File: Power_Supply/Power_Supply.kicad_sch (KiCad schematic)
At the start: 62 parts, among them J1 ICSP, J2 Conn_01x01, J3 Conn_01x01, J4 Conn_01x02, SW1 UP, SW2 DW, SW3 V_I_SEL, SW4 O_EN, U1 L78L08_SOT89, U2 ATmega328PB-AU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

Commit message: schematic general changes
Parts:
- gave numbers to parts that had none: 1
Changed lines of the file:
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@@
   (symbol (lib_id "power:+5V") (at 177.8 130.81 0) (unit 1)
     (in_bom yes) (on_board yes)
-    (property "Reference" "#PWR?" (id 0) (at 177.8 134.62 0)
+    (property "Reference" "#PWR0138" (id 0) (at 177.8 134.62 0)
       (effects (font (size 1.27 1.27)) hide)
     )
@@
   (symbol (lib_id "power:GND") (at 172.72 133.35 0) (unit 1)
     (in_bom yes) (on_board yes)
-    (property "Reference" "#PWR?" (id 0) (at 172.72 139.7 0)
+    (property "Reference" "#PWR0139" (id 0) (at 172.72 139.7 0)
       (effects (font (size 1.27 1.27)) hide)
     )
@@
   (symbol (lib_id "Connector_Generic:Conn_01x07") (at 187.96 140.97 0) (unit 1)
     (in_bom yes) (on_board yes)
-    (property "Reference" "J?" (id 0) (at 190.5 139.7 0)
+    (property "Reference" "J5" (id 0) (at 190.5 139.7 0)
       (effects (font (size 1.27 1.27)) (justify left))
     )
@@
     )
     (path "/4d9958f2-beb5-4ed4-8a98-4e96ac27dafe"
-      (reference "#PWR?") (unit 1)
+      (reference "#PWR0138") (unit 1)
     )
     (path "/62210738-7293-4785-87bd-dc34d7328707"
-      (reference "#PWR?") (unit 1)
+      (reference "#PWR0139") (unit 1)
     )
     (path "/a216915c-7324-469c-8737-2c3edfb6ea67"
@@
     )
     (path "/4a5aceff-e57e-435c-ba37-61c44454879c"
-      (reference "J?") (unit 1)
+      (reference "J5") (unit 1)
     )
     (path "/93bb1d96-5265-4922-b320-5a7c229c525d"

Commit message: layout complete - OLED missing
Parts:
- removed C12, C7: 100nF, Capacitor_SMD:C_0805_2012Metric, symbol Device:C_Small
- removed J4: Conn_01x02, Custom_Vertical_1x_2.54mm_Pin_Header:PinHeader_1x02_P2.54mm_Vertical, symbol Connector_Generic:Conn_01x02
- added C? (x2): 10uF, Capacitor_SMD:C_Elec_5x5.4, symbol Device:CP_Small
- added H1, H2, H3, H4: MountingHole_Pad, MountingHole:MountingHole_2.2mm_M2_ISO7380_Pad, symbol Mechanical:MountingHole_Pad
- added J4: Screw_Terminal_01x02, TerminalBlock_Altech:Altech_AK300_1x02_P5.00mm_45-Degree, symbol Connector:Screw_Terminal_01x02
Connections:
- net SCL1 is gone; now on net SW4: U2.6 (PE1)
- net SDA1 is gone; now on net SW1: U2.3 (PE0)
- net +VSW: now also C?.2, J4.1 (Pin_1)
- net GND: now also C?.1, C?.1, H1.1, H2.1, H3.1, H4.1, J4.2 (Pin_2)
- net VDC: now also C?.2
- net SW1: now reaches R6.2, SW1.1
- net SW1: no longer U2.1 (PD3)
- net SW2: now reaches R8.2, SW2.1, U2.2 (PD4)
- net SW4: now reaches R10.2, SW4.1
- net SW4: no longer U2.10 (PD6)
- net SW3: now reaches R9.2, SW3.1
- net SW3: now also U2.1 (PD3); no longer U2.9 (PD5)

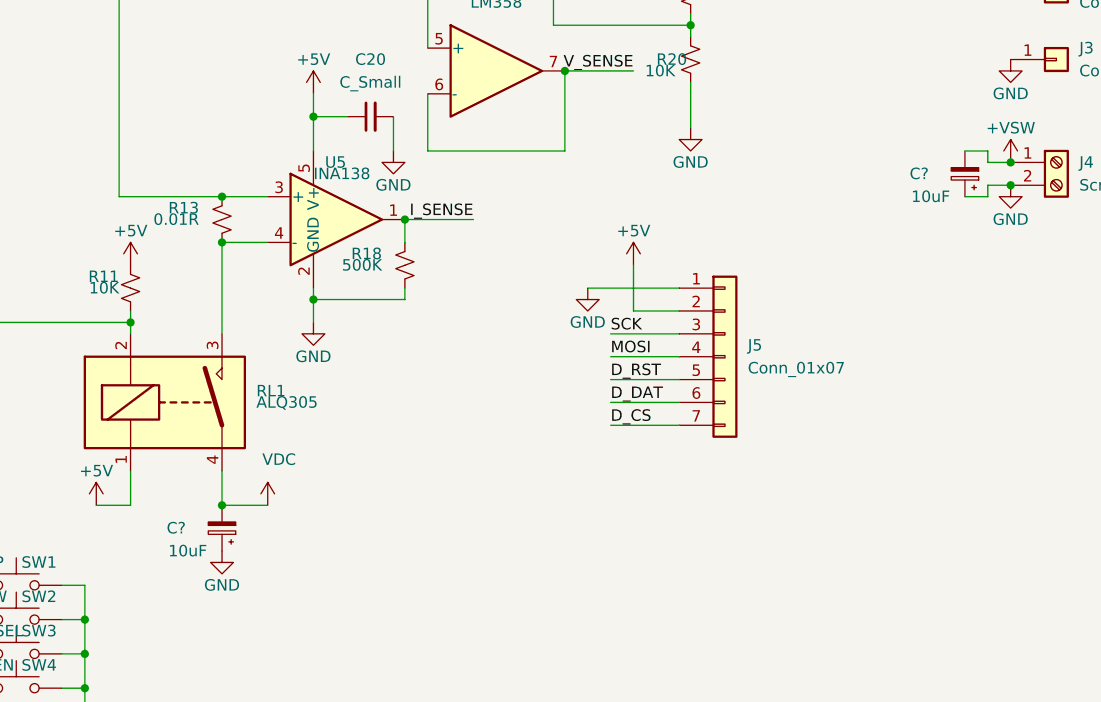
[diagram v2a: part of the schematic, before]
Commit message: schem - added bypass caps
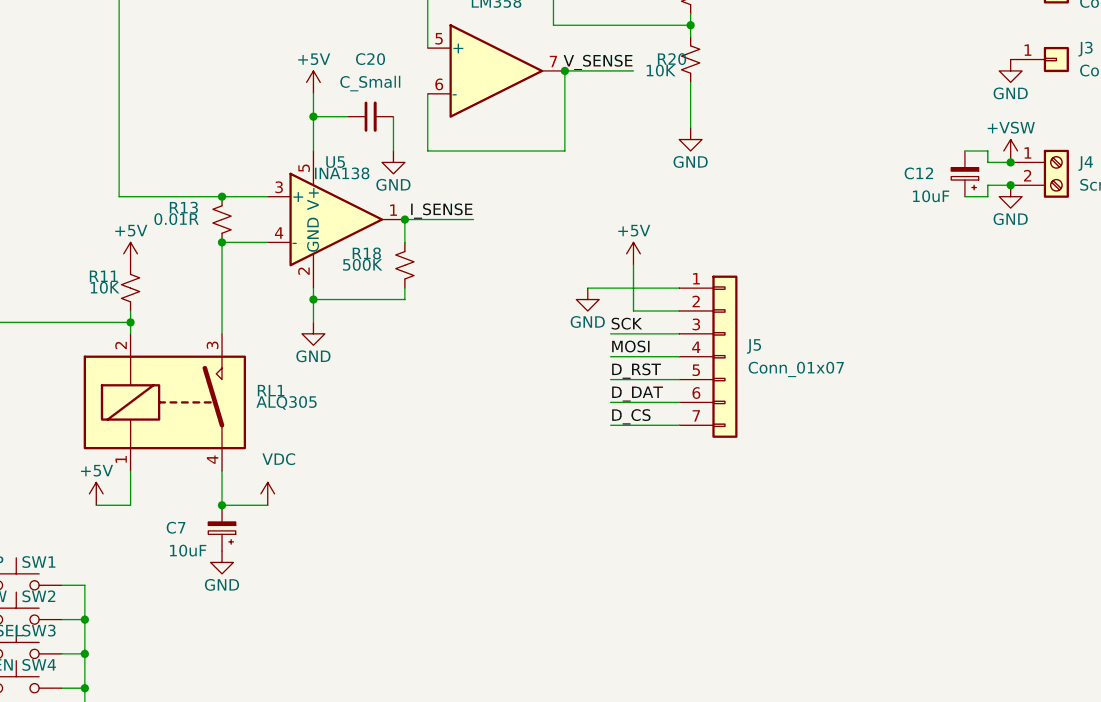
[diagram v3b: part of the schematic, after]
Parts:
- gave numbers to parts that had none: 2
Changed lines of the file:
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@@
   (symbol (lib_id "power:GND") (at 132.08 162.56 0) (unit 1)
     (in_bom yes) (on_board yes)
-    (property "Reference" "#PWR?" (id 0) (at 132.08 168.91 0)
+    (property "Reference" "#PWR0141" (id 0) (at 132.08 168.91 0)
       (effects (font (size 1.27 1.27)) hide)
     )
@@
   (symbol (lib_id "Device:CP_Small") (at 132.08 160.02 180) (unit 1)
     (in_bom yes) (on_board yes)
-    (property "Reference" "C?" (id 0) (at 127 160.02 0))
+    (property "Reference" "C7" (id 0) (at 127 160.02 0))
     (property "Value" "10uF" (id 1) (at 128.27 162.56 0))
     (property "Footprint" "Capacitor_SMD:C_Elec_5x5.4" (id 2) (at 132.08 160.02 0)
@@
   (symbol (lib_id "Device:CP_Small") (at 214.63 120.65 180) (unit 1)
     (in_bom yes) (on_board yes)
-    (property "Reference" "C?" (id 0) (at 209.55 120.65 0))
+    (property "Reference" "C12" (id 0) (at 209.55 120.65 0))
     (property "Value" "10uF" (id 1) (at 210.82 123.19 0))
     (property "Footprint" "Capacitor_SMD:C_Elec_5x5.4" (id 2) (at 214.63 120.65 0)
@@
     )
     (path "/255a29b3-3ad0-4a90-bdf9-643315723593"
-      (reference "#PWR?") (unit 1)
+      (reference "#PWR0141") (unit 1)
     )
     (path "/a216915c-7324-469c-8737-2c3edfb6ea67"
@@
       (reference "C6") (unit 1)
     )
+    (path "/311ae82b-454a-4b31-a9dc-b6314a74ab0d"
+      (reference "C7") (unit 1)
+    )
     (path "/232dade7-711c-48f9-ad1c-1fae503ac0aa"
       (reference "C8") (unit 1)
@@
       (reference "C11") (unit 1)
     )
+    (path "/80312307-f61e-439d-8183-53fd4206ff5b"
+      (reference "C12") (unit 1)
+    )
     (path "/e9f98593-5eac-4a3a-82ed-b73c53af7d03"
       (reference "C13") (unit 1)
@@
       (reference "C21") (unit 1)
     )
-    (path "/311ae82b-454a-4b31-a9dc-b6314a74ab0d"
-      (reference "C?") (unit 1)
-    )
-    (path "/80312307-f61e-439d-8183-53fd4206ff5b"
-      (reference "C?") (unit 1)
-    )
     (path "/b02026a8-7dc6-42d3-9812-c38db0931d18"

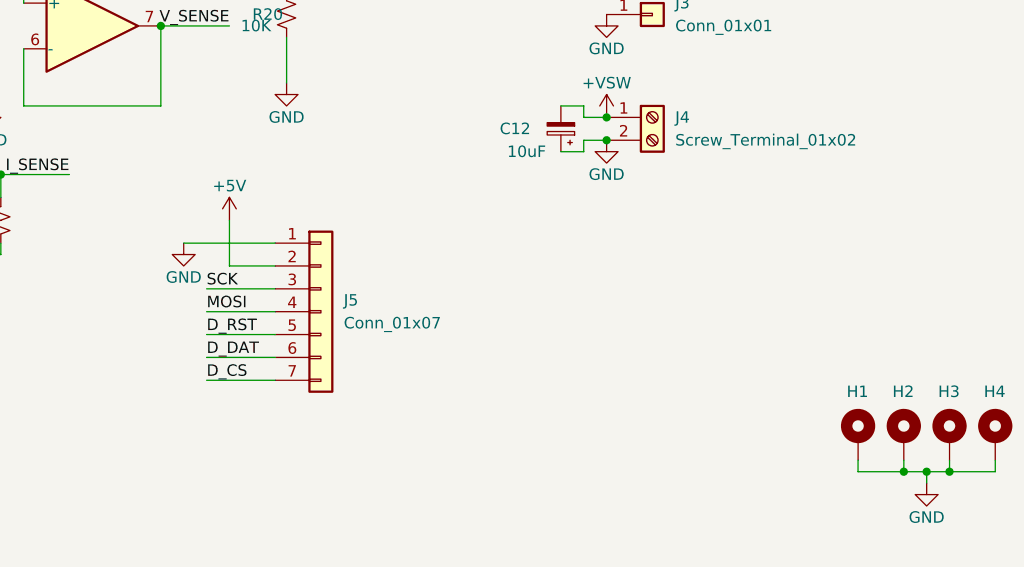
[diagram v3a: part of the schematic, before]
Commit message: did via stitching for ground
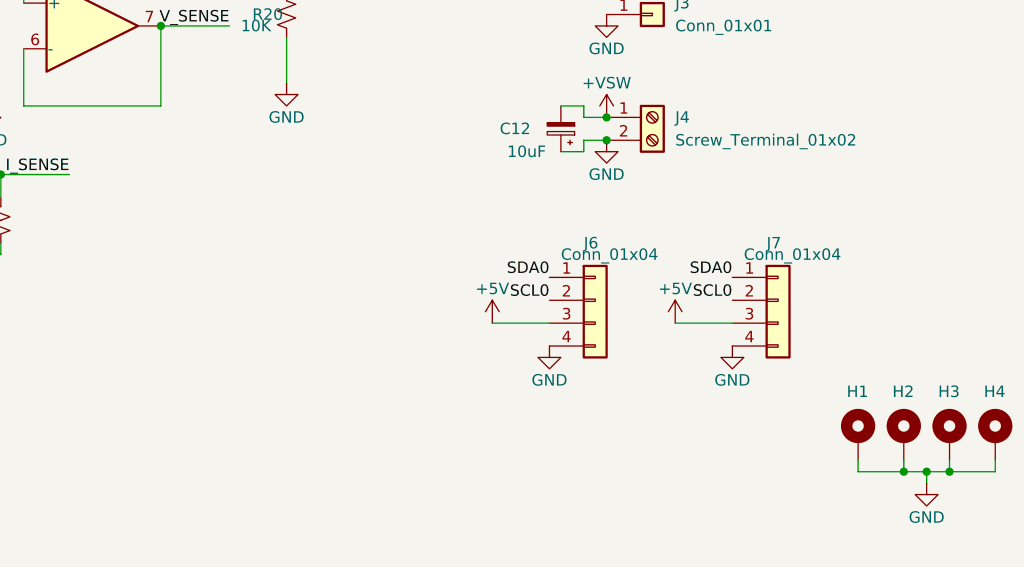
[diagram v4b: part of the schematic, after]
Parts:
- removed J5: Conn_01x07, Custom_Vertical_1x_2.54mm_Pin_Header:PinHeader_1x07_P2.54mm_Vertical, symbol Connector_Generic:Conn_01x07
- added J6, J7: Conn_01x04, Custom_Vertical_1x_2.54mm_Pin_Header:PinHeader_1x04_P2.54mm_Vertical, symbol Connector_Generic:Conn_01x04
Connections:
- net +5V: now also J6.3 (Pin_3), J7.3 (Pin_3)
- net GND: now also J6.4 (Pin_4), J7.4 (Pin_4)
- net SCL0: now also J6.2 (Pin_2), J7.2 (Pin_2)
- net SDA0: now also J6.1 (Pin_1), J7.1 (Pin_1)
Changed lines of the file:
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@@
-    (stroke (width 0) (type solid) (color 0 0 0 0))
-  )
-  (wire (pts (xy 172.72 133.35) (xy 182.88 133.35))
-    (stroke (width 0) (type solid) (color 0 0 0 0))
-  )
-  (wire (pts (xy 175.26 138.43) (xy 182.88 138.43))
-    (stroke (width 0) (type solid) (color 0 0 0 0))
-  )
-  (wire (pts (xy 175.26 140.97) (xy 182.88 140.97))
-    (stroke (width 0) (type solid) (color 0 0 0 0))
-  )
-  (wire (pts (xy 175.26 143.51) (xy 182.88 143.51))
-    (stroke (width 0) (type solid) (color 0 0 0 0))
-  )
-  (wire (pts (xy 175.26 146.05) (xy 182.88 146.05))
-    (stroke (width 0) (type solid) (color 0 0 0 0))
-  )
-  (wire (pts (xy 175.26 148.59) (xy 182.88 148.59))
     (stroke (width 0) (type solid) (color 0 0 0 0))
   )
@@
     (stroke (width 0) (type solid) (color 0 0 0 0))
   )
-  (wire (pts (xy 177.8 130.81) (xy 177.8 135.89))
-    (stroke (width 0) (type solid) (color 0 0 0 0))
-  )
-  (wire (pts (xy 177.8 135.89) (xy 182.88 135.89))
-    (stroke (width 0) (type solid) (color 0 0 0 0))
-  )
   (wire (pts (xy 179.07 53.34) (xy 179.07 55.88))
     (stroke (width 0) (type solid) (color 0 0 0 0))
@@
     (stroke (width 0) (type solid) (color 0 0 0 0))
   )
+  (wire (pts (xy 207.01 142.24) (xy 213.36 142.24))
+    (stroke (width 0) (type solid) (color 0 0 0 0))
+  )
   (wire (pts (xy 214.63 118.11) (xy 217.17 118.11))
     (stroke (width 0) (type solid) (color 0 0 0 0))
@@
   )
   (wire (pts (xy 217.17 123.19) (xy 217.17 121.92))
+    (stroke (width 0) (type solid) (color 0 0 0 0))
+  )
+  (wire (pts (xy 227.33 142.24) (xy 233.68 142.24))
     (stroke (width 0) (type solid) (color 0 0 0 0))
   )
@@
     (effects (font (size 1.27 1.27)) (justify right bottom))
   )
-  (label "SCK" (at 175.26 138.43 0)
-    (effects (font (size 1.27 1.27)) (justify left bottom))
-  )
-  (label "MOSI" (at 175.26 140.97 0)
-    (effects (font (size 1.27 1.27)) (justify left bottom))
-  )
-  (label "D_RST" (at 175.26 143.51 0)
-    (effects (font (size 1.27 1.27)) (justify left bottom))
-  )
-  (label "D_DAT" (at 175.26 146.05 0)
-    (effects (font (size 1.27 1.27)) (justify left bottom))
-  )
-  (label "D_CS" (at 175.26 148.59 0)
-    (effects (font (size 1.27 1.27)) (justify left bottom))
-  )
   (label "V_SENSE" (at 177.8 109.22 180)
     (effects (font (size 1.27 1.27)) (justify right bottom))
@@
   )
   (label "~POT_CS" (at 194.31 71.12 180)
+    (effects (font (size 1.27 1.27)) (justify right bottom))
+  )
+  (label "SDA0" (at 213.36 137.16 180)
+    (effects (font (size 1.27 1.27)) (justify right bottom))
+  )
+  (label "SCL0" (at 213.36 139.7 180)
+    (effects (font (size 1.27 1.27)) (justify right bottom))
+  )
+  (label "SDA0" (at 233.68 137.16 180)
+    (effects (font (size 1.27 1.27)) (justify right bottom))
+  )
+  (label "SCL0" (at 233.68 139.7 180)
     (effects (font (size 1.27 1.27)) (justify right bottom))
   )
@@
     )
   )
-  (symbol (lib_id "power:+5V") (at 177.8 130.81 0) (unit 1)
-    (in_bom yes) (on_board yes)
-    (property "Reference" "#PWR0138" (id 0) (at 177.8 134.62 0)
-      (effects (font (size 1.27 1.27)) hide)
-    )
-    (property "Value" "+5V" (id 1) (at 177.8 127 0))
-    (property "Footprint" "" (id 2) (at 177.8 130.81 0)
-      (effects (font (size 1.27 1.27)) hide)
-    )
-    (property "Datasheet" "" (id 3) (at 177.8 130.81 0)
-      (effects (font (size 1.27 1.27)) hide)
-    )
-  )
   (symbol (lib_id "power:+5V") (at 179.07 53.34 0) (unit 1)
     (in_bom yes) (on_board yes)
@@
     )
   )
+  (symbol (lib_id "power:+5V") (at 207.01 142.24 0) (unit 1)
+    (in_bom yes) (on_board yes)
+    (property "Reference" "#PWR0142" (id 0) (at 207.01 146.05 0)
+      (effects (font (size 1.27 1.27)) hide)
+    )
+    (property "Value" "+5V" (id 1) (at 207.01 138.43 0))
+    (property "Footprint" "" (id 2) (at 207.01 142.24 0)
+      (effects (font (size 1.27 1.27)) hide)
+    )
+    (property "Datasheet" "" (id 3) (at 207.01 142.24 0)
+      (effects (font (size 1.27 1.27)) hide)
+    )
+  )
   (symbol (lib_id "power:VDC") (at 219.71 100.33 0) (unit 1)
     (in_bom yes) (on_board yes)
@@
     )
   )
+  (symbol (lib_id "power:+5V") (at 227.33 142.24 0) (unit 1)
+    (in_bom yes) (on_board yes)
+    (property "Reference" "#PWR0145" (id 0) (at 227.33 146.05 0)
+      (effects (font (size 1.27 1.27)) hide)
+    )
+    (property "Value" "+5V" (id 1) (at 227.33 138.43 0))
+    (property "Footprint" "" (id 2) (at 227.33 142.24 0)
+      (effects (font (size 1.27 1.27)) hide)
+    )
+    (property "Datasheet" "" (id 3) (at 227.33 142.24 0)
+      (effects (font (size 1.27 1.27)) hide)
+    )
+  )
   (symbol (lib_id "power:GND") (at 26.67 118.11 0) (unit 1)
     (in_bom yes) (on_board yes)
@@
     )
   )
-  (symbol (lib_id "power:GND") (at 172.72 133.35 0) (unit 1)
-    (in_bom yes) (on_board yes)
-    (property "Reference" "#PWR0139" (id 0) (at 172.72 139.7 0)
-      (effects (font (size 1.27 1.27)) hide)
-    )
-    (property "Value" "GND" (id 1) (at 172.72 137.16 0))
-    (property "Footprint" "" (id 2) (at 172.72 133.35 0)
-      (effects (font (size 1.27 1.27)) hide)
-    )
-    (property "Datasheet" "" (id 3) (at 172.72 133.35 0)
-      (effects (font (size 1.27 1.27)) hide)
-    )
-  )
   (symbol (lib_id "power:GND") (at 176.53 80.01 0) (unit 1)
     (in_bom yes) (on_board yes)
@@
     )
   )
+  (symbol (lib_id "power:GND") (at 213.36 144.78 0) (unit 1)
+    (in_bom yes) (on_board yes)
+    (property "Reference" "#PWR0143" (id 0) (at 213.36 151.13 0)
+      (effects (font (size 1.27 1.27)) hide)
+    )
+    (property "Value" "GND" (id 1) (at 213.36 148.59 0))
+    (property "Footprint" "" (id 2) (at 213.36 144.78 0)
+      (effects (font (size 1.27 1.27)) hide)
+    )
+    (property "Datasheet" "" (id 3) (at 213.36 144.78 0)
+      (effects (font (size 1.27 1.27)) hide)
+    )
+  )
   (symbol (lib_id "power:GND") (at 219.71 107.95 0) (unit 1)
     (in_bom yes) (on_board yes)
@@
     )
     (property "Datasheet" "" (id 3) (at 219.71 121.92 0)
+      (effects (font (size 1.27 1.27)) hide)
+    )
+  )
+  (symbol (lib_id "power:GND") (at 233.68 144.78 0) (unit 1)
+    (in_bom yes) (on_board yes)
+    (property "Reference" "#PWR0144" (id 0) (at 233.68 151.13 0)
+      (effects (font (size 1.27 1.27)) hide)
+    )
+    (property "Value" "GND" (id 1) (at 233.68 148.59 0))
+    (property "Footprint" "" (id 2) (at 233.68 144.78 0)
+      (effects (font (size 1.27 1.27)) hide)
+    )
+    (property "Datasheet" "" (id 3) (at 233.68 144.78 0)
       (effects (font (size 1.27 1.27)) hide)
     )
@@
     )
   )
+  (symbol (lib_id "Connector_Generic:Conn_01x04") (at 218.44 139.7 0) (unit 1)
+    (in_bom yes) (on_board yes)
+    (property "Reference" "J6" (id 0) (at 217.17 133.35 0)
+      (effects (font (size 1.27 1.27)) (justify left))
+    )
+    (property "Value" "Conn_01x04" (id 1) (at 214.63 134.62 0)
+      (effects (font (size 1.27 1.27)) (justify left))
+    )
+    (property "Footprint" "Custom_Vertical_1x_2.54mm_Pin_Header:PinHeader_1x04_P2.54mm_Vertical" (id 2) (at 218.44 139.7 0)
+      (effects (font (size 1.27 1.27)) hide)
+    )
+    (property "Datasheet" "~" (id 3) (at 218.44 139.7 0)
+      (effects (font (size 1.27 1.27)) hide)
+    )
+  )
+  (symbol (lib_id "Connector_Generic:Conn_01x04") (at 238.76 139.7 0) (unit 1)
+    (in_bom yes) (on_board yes)
+    (property "Reference" "J7" (id 0) (at 237.49 133.35 0)
+      (effects (font (size 1.27 1.27)) (justify left))
+    )
+    (property "Value" "Conn_01x04" (id 1) (at 234.95 134.62 0)
+      (effects (font (size 1.27 1.27)) (justify left))
+    )
+    (property "Footprint" "Custom_Vertical_1x_2.54mm_Pin_Header:PinHeader_1x04_P2.54mm_Vertical" (id 2) (at 238.76 139.7 0)
+      (effects (font (size 1.27 1.27)) hide)
+    )
+    (property "Datasheet" "~" (id 3) (at 238.76 139.7 0)
+      (effects (font (size 1.27 1.27)) hide)
+    )
+  )
   (symbol (lib_id "Connector_Generic:Conn_02x03_Odd_Even") (at 88.9 114.3 0) (unit 1)
     (in_bom yes) (on_board yes)
@@
     )
     (property "Datasheet" "~" (id 3) (at 88.9 114.3 0)
-      (effects (font (size 1.27 1.27)) hide)
-    )
-  )
-  (symbol (lib_id "Connector_Generic:Conn_01x07") (at 187.96 140.97 0) (unit 1)
-    (in_bom yes) (on_board yes)
-    (property "Reference" "J5" (id 0) (at 190.5 139.7 0)
-      (effects (font (size 1.27 1.27)) (justify left))
-    )
-    (property "Value" "Conn_01x07" (id 1) (at 190.5 142.24 0)
-      (effects (font (size 1.27 1.27)) (justify left))
-    )
-    (property "Footprint" "Custom_Vertical_1x_2.54mm_Pin_Header:PinHeader_1x07_P2.54mm_Vertical" (id 2) (at 187.96 140.97 0)
-      (effects (font (size 1.27 1.27)) hide)
-    )
-    (property "Datasheet" "~" (id 3) (at 187.96 140.97 0)
       (effects (font (size 1.27 1.27)) hide)
     )
@@
       (reference "#PWR0137") (unit 1)
     )
-    (path "/4d9958f2-beb5-4ed4-8a98-4e96ac27dafe"
-      (reference "#PWR0138") (unit 1)
-    )
-    (path "/62210738-7293-4785-87bd-dc34d7328707"
-      (reference "#PWR0139") (unit 1)
-    )
     (path "/67d38491-11d8-4ac9-9ec2-2317110a7fb9"
       (reference "#PWR0140") (unit 1)
@@
       (reference "#PWR0141") (unit 1)
     )
+    (path "/0ebb59e0-4acf-450d-98d1-28d5ddd3d832"
+      (reference "#PWR0142") (unit 1)
+    )
+    (path "/0b268c81-cce1-4cb4-9f9d-1bb87afa4a6c"
+      (reference "#PWR0143") (unit 1)
+    )
+    (path "/70e95788-6272-448e-8fa7-7d4ad15c97df"
+      (reference "#PWR0144") (unit 1)
+    )
+    (path "/726b5d41-9982-4dfa-951e-238a8d45e032"
+      (reference "#PWR0145") (unit 1)
+    )
     (path "/a216915c-7324-469c-8737-2c3edfb6ea67"
       (reference "C1") (unit 1)
@@
       (reference "J4") (unit 1)
     )
-    (path "/4a5aceff-e57e-435c-ba37-61c44454879c"
-      (reference "J5") (unit 1)
+    (path "/fa1b73a3-58fa-4300-9c36-ee8a35a7c023"
+      (reference "J6") (unit 1)
+    )
+    (path "/344d620a-4c63-4dc3-8e90-cc14d3ea26f4"
+      (reference "J7") (unit 1)
     )
     (path "/93bb1d96-5265-4922-b320-5a7c229c525d"
